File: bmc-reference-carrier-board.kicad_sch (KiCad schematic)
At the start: 0 parts

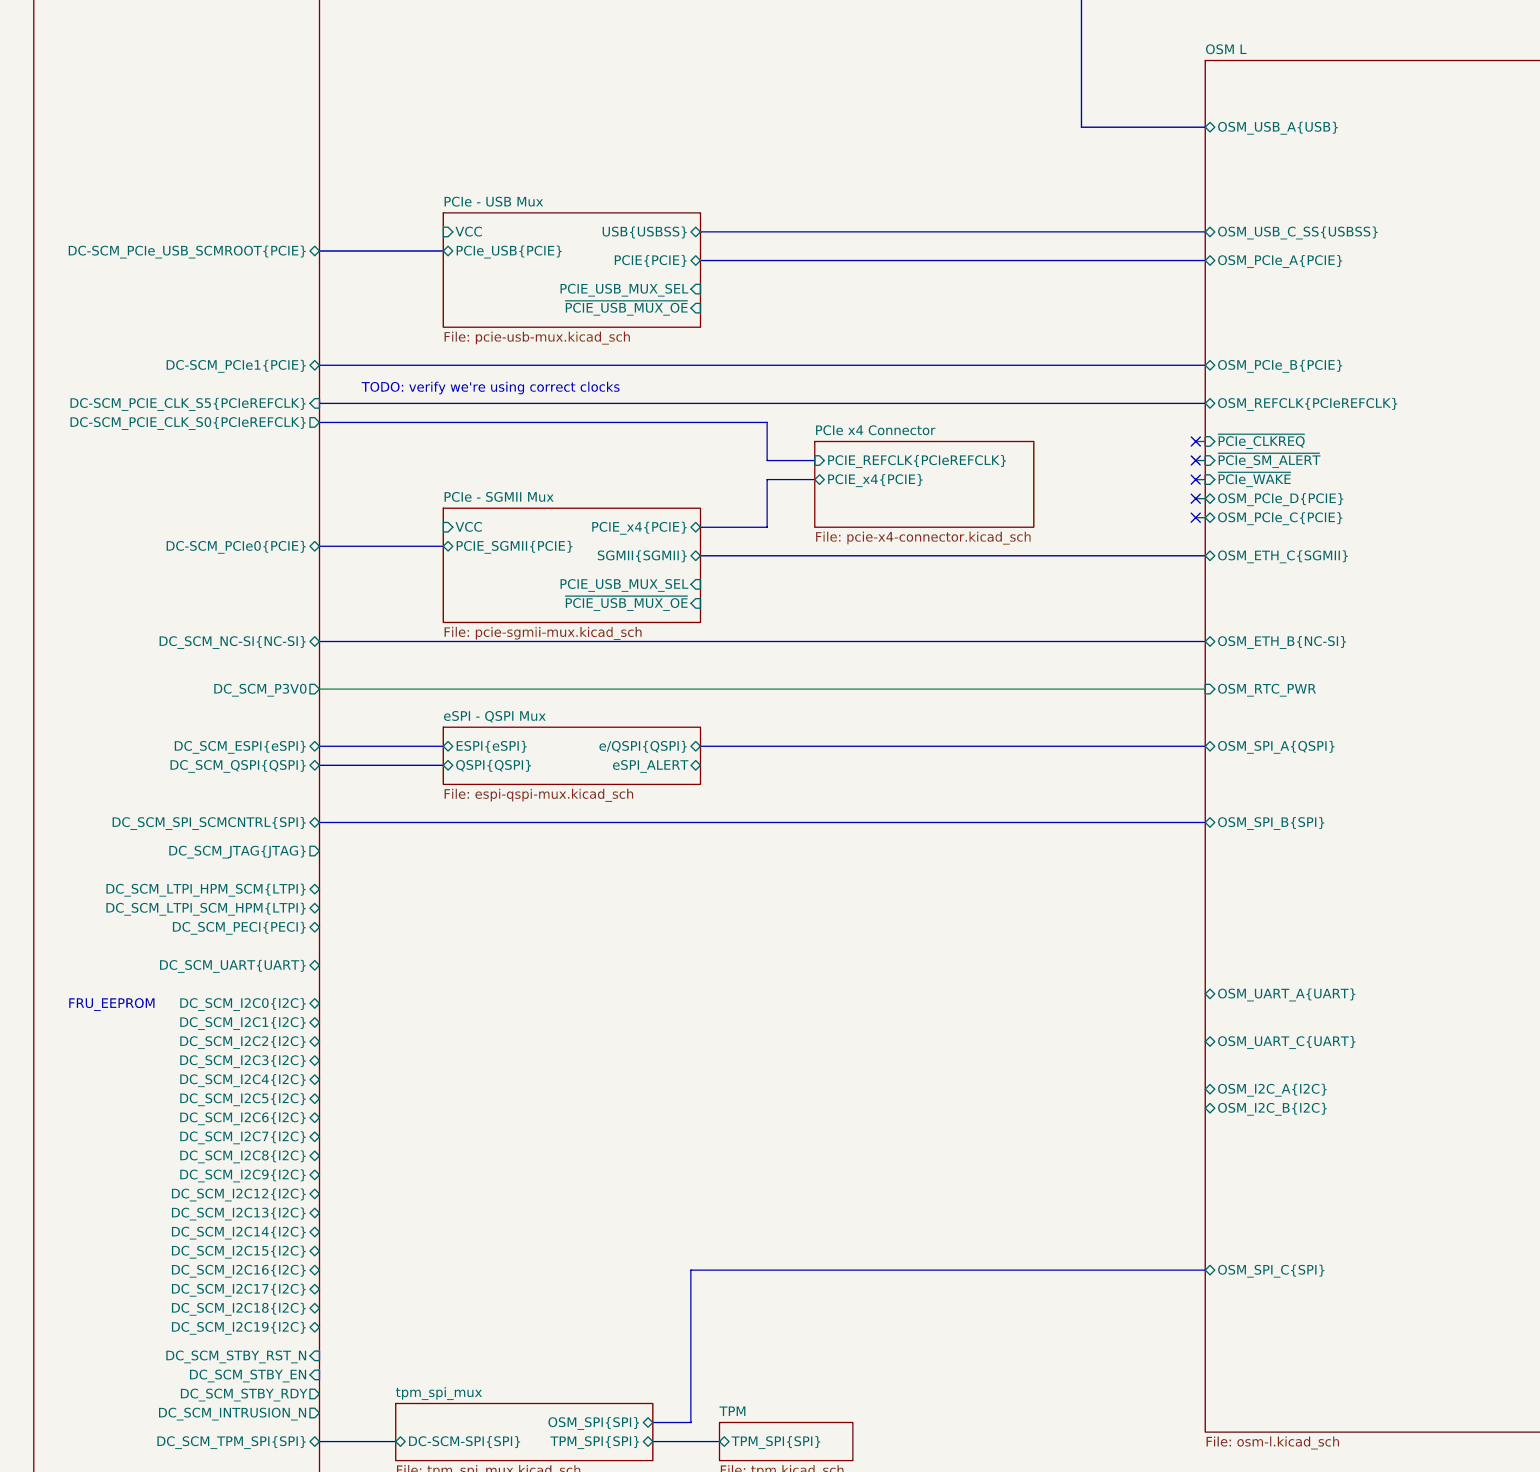
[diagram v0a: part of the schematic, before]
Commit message: [#82323] Add PCIeREFCLK bus, update DC-SCM labels
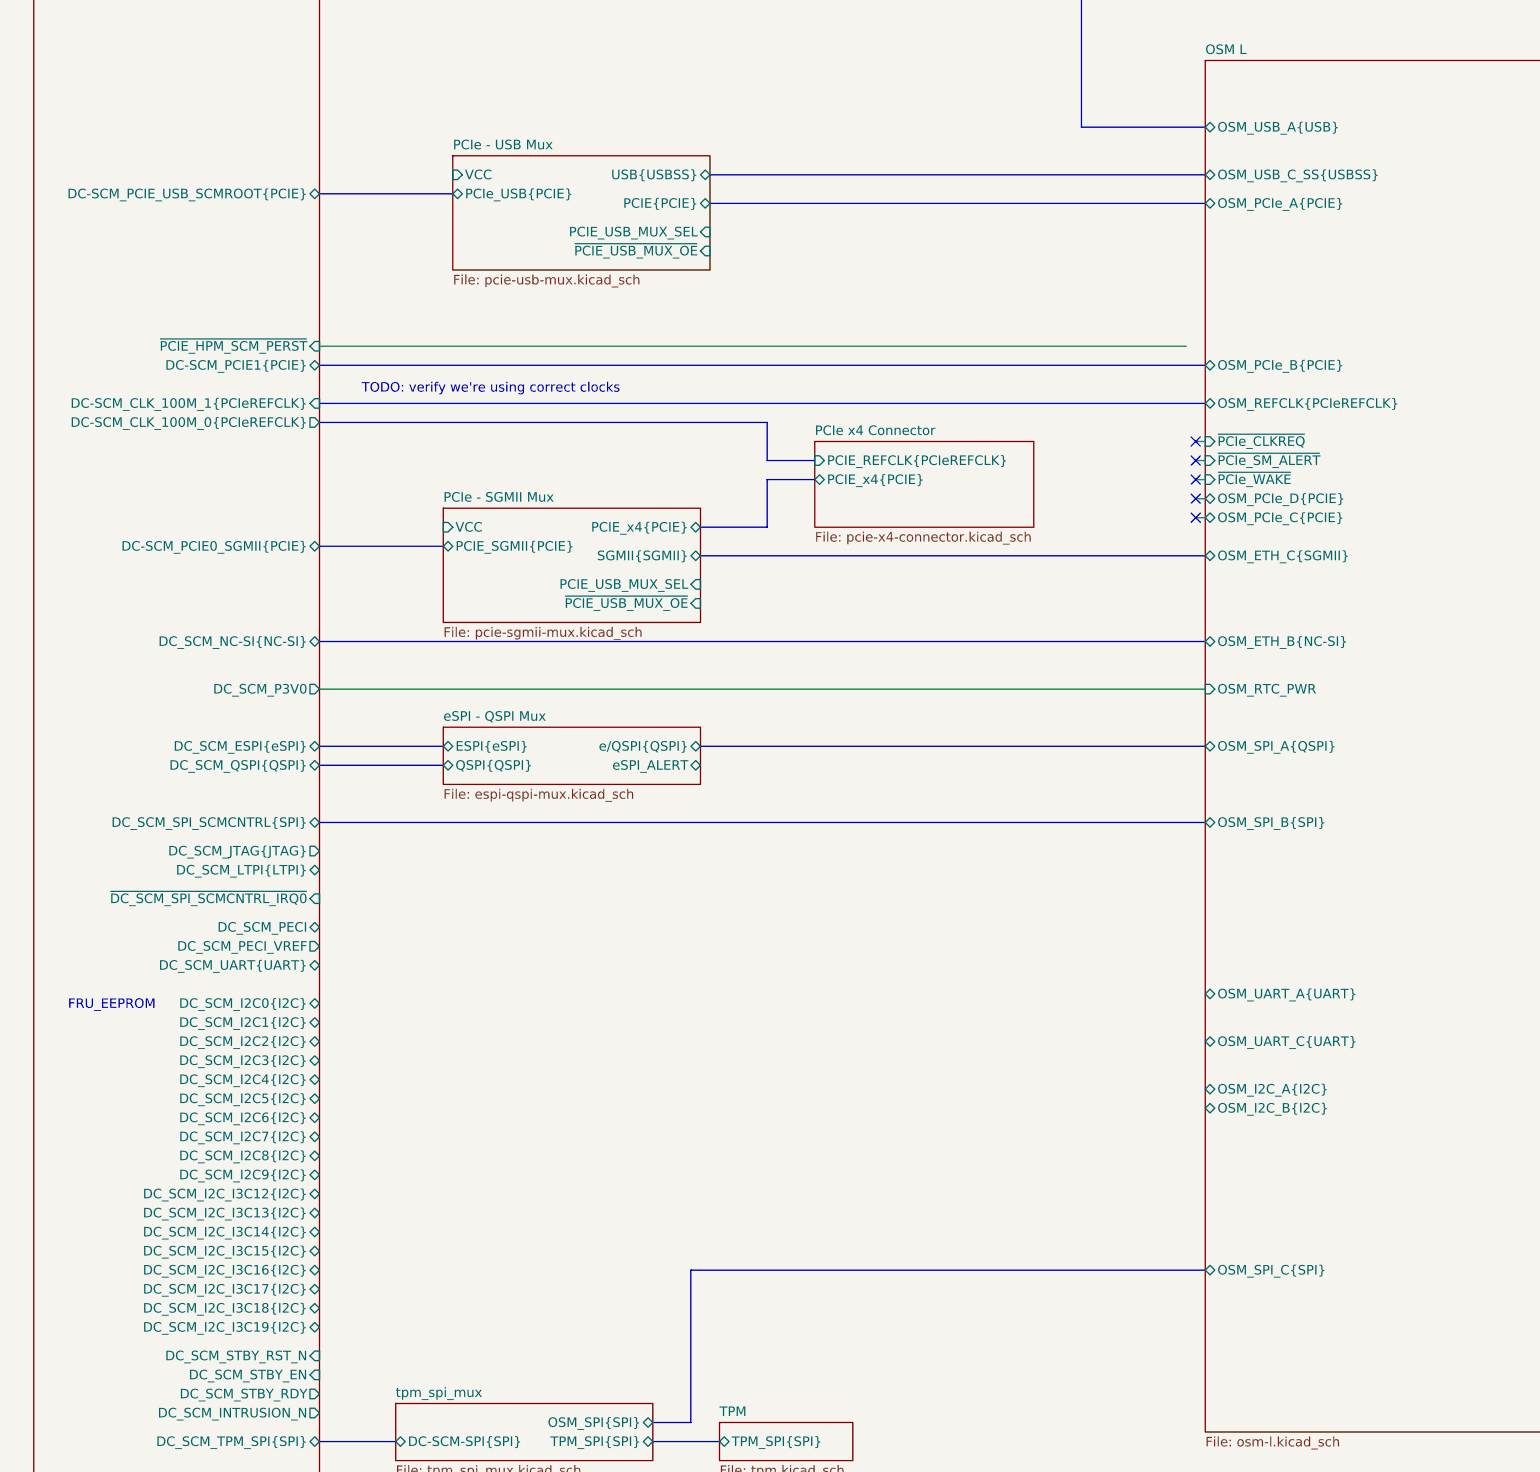
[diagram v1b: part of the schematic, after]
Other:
- sheet DC-SCM 2.1 connector ports: added DC-SCM_CLK_100M_0{PCIeREFCLK}, DC-SCM_CLK_100M_1{PCIeREFCLK}, DC-SCM_PCIE0_SGMII{PCIE}, DC-SCM_PCIE1{PCIE}, DC-SCM_PCIE_USB_SCMROOT{PCIE}, DC_SCM_I2C_I3C12{I2C}, DC_SCM_I2C_I3C13{I2C}, DC_SCM_I2C_I3C14{I2C}, DC_SCM_I2C_I3C15{I2C}, DC_SCM_I2C_I3C16{I2C}, DC_SCM_I2C_I3C17{I2C}, DC_SCM_I2C_I3C18{I2C}, DC_SCM_I2C_I3C19{I2C}, DC_SCM_LTPI{LTPI}, DC_SCM_PECI, DC_SCM_PECI_VREF, ~{DC_SCM_SPI_SCMCNTRL_IRQ0}, ~{PCIE_HPM_SCM_PERST}; removed DC-SCM_PCIE_CLK_S0{PCIeREFCLK}, DC-SCM_PCIE_CLK_S5{PCIeREFCLK}, DC-SCM_PCIe0{PCIE}, DC-SCM_PCIe1{PCIE}, DC-SCM_PCIe_USB_SCMROOT{PCIE}, DC_SCM_I2C12{I2C}, DC_SCM_I2C13{I2C}, DC_SCM_I2C14{I2C}, DC_SCM_I2C15{I2C}, DC_SCM_I2C16{I2C}, DC_SCM_I2C17{I2C}, DC_SCM_I2C18{I2C}, DC_SCM_I2C19{I2C}, DC_SCM_LTPI_HPM_SCM{LTPI}, DC_SCM_LTPI_SCM_HPM{LTPI}, DC_SCM_PECI{PECI}
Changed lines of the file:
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@@
 		)
+	)
+	(bus_alias "PCIeREFCLK"
+		(members "CLK+" "CLK-")
 	)
 	(bus_alias "QSPI"
@@
 	(bus
 		(pts
-			(xy 109.22 109.22) (xy 176.53 109.22)
+			(xy 110.49 101.6) (xy 176.53 101.6)
 		)
 		(stroke
@@
 		)
 	)
-	(bus
-		(pts
-			(xy 58.42 111.76) (xy 74.93 111.76)
+	(wire
+		(pts
+			(xy 58.42 124.46) (xy 173.99 124.46)
+		)
+		(stroke
+			(width 0)
+			(type default)
+		)
+	)
+	(bus
+		(pts
+			(xy 58.42 104.14) (xy 76.2 104.14)
 		)
 		(stroke
@@
 	(bus
 		(pts
-			(xy 109.22 113.03) (xy 176.53 113.03)
+			(xy 110.49 105.41) (xy 176.53 105.41)
 		)
 		(stroke
@@
 	)
 	(sheet
-		(at 74.93 106.68)
+		(at 76.2 99.06)
 		(size 34.29 15.24)
 		(exclude_from_sim no)
@@
 		)
 		(property "Sheetname" "PCIe - USB Mux"
-			(at 74.93 105.9684 0)
+			(at 76.2 98.3484 0)
 			(effects
 				(font
@@
 		)
 		(property "Sheetfile" "pcie-usb-mux.kicad_sch"
-			(at 74.93 122.5046 0)
+			(at 76.2 114.8846 0)
 			(effects
 				(font
@@
 		)
 		(pin "PCIE{PCIE}" bidirectional
-			(at 109.22 113.03 0)
+			(at 110.49 105.41 0)
 			(effects
 				(font
@@
 		)
 		(pin "PCIe_USB{PCIE}" bidirectional
-			(at 74.93 111.76 180)
+			(at 76.2 104.14 180)
 			(effects
 				(font
@@
 		)
 		(pin "USB{USBSS}" bidirectional
-			(at 109.22 109.22 0)
+			(at 110.49 101.6 0)
 			(effects
 				(font
@@
 		)
 		(pin "PCIE_USB_MUX_SEL" input
-			(at 109.22 116.84 0)
+			(at 110.49 109.22 0)
 			(effects
 				(font
@@
 		)
 		(pin "~{PCIE_USB_MUX_OE}" input
-			(at 109.22 119.38 0)
+			(at 110.49 111.76 0)
 			(effects
 				(font
@@
 		)
 		(pin "VCC" input
-			(at 74.93 109.22 180)
+			(at 76.2 101.6 180)
 			(effects
 				(font
@@
 		)
 		(pin "OSM_PCIe_A{PCIE}" bidirectional
-			(at 176.53 113.03 180)
+			(at 176.53 105.41 180)
 			(effects
 				(font
@@
 		)
 		(pin "OSM_USB_C_SS{USBSS}" bidirectional
-			(at 176.53 109.22 180)
+			(at 176.53 101.6 180)
 			(effects
 				(font
@@
 			)
 		)
-		(pin "DC_SCM_I2C13{I2C}" bidirectional
-			(at 58.42 240.03 0)
-			(effects
-				(font
-					(size 1.27 1.27)
-				)
-				(justify right)
-			)
-		)
 		(pin "DC_SCM_I2C5{I2C}" bidirectional
 			(at 58.42 224.79 0)
@@
 			)
 		)
-		(pin "DC_SCM_I2C12{I2C}" bidirectional
-			(at 58.42 237.49 0)
-			(effects
-				(font
-					(size 1.27 1.27)
-				)
-				(justify right)
-			)
-		)
-		(pin "DC_SCM_LTPI_SCM_HPM{LTPI}" bidirectional
-			(at 58.42 199.39 0)
-			(effects
-				(font
-					(size 1.27 1.27)
-				)
-				(justify right)
-			)
-		)
-		(pin "DC_SCM_LTPI_HPM_SCM{LTPI}" bidirectional
-			(at 58.42 196.85 0)
-			(effects
-				(font
-					(size 1.27 1.27)
-				)
-				(justify right)
-			)
-		)
 		(pin "DC_SCM_ESPI{eSPI}" bidirectional
 			(at 58.42 177.8 0)
@@
 			)
 		)
-		(pin "DC_SCM_PECI{PECI}" bidirectional
-			(at 58.42 201.93 0)
-			(effects
-				(font
-					(size 1.27 1.27)
-				)
-				(justify right)
-			)
-		)
 		(pin "DC_SCM_USB1{USB}" bidirectional
 			(at 58.42 34.29 0)
@@
 			)
 		)
-		(pin "DC_SCM_I2C14{I2C}" bidirectional
-			(at 58.42 242.57 0)
-			(effects
-				(font
-					(size 1.27 1.27)
-				)
-				(justify right)
-			)
-		)
-		(pin "DC_SCM_I2C15{I2C}" bidirectional
-			(at 58.42 245.11 0)
-			(effects
-				(font
-					(size 1.27 1.27)
-				)
-				(justify right)
-			)
-		)
-		(pin "DC_SCM_I2C16{I2C}" bidirectional
-			(at 58.42 247.65 0)
-			(effects
-				(font
-					(size 1.27 1.27)
-				)
-				(justify right)
-			)
-		)
-		(pin "DC_SCM_I2C17{I2C}" bidirectional
-			(at 58.42 250.19 0)
-			(effects
-				(font
-					(size 1.27 1.27)
-				)
-				(justify right)
-			)
-		)
-		(pin "DC_SCM_I2C18{I2C}" bidirectional
-			(at 58.42 252.73 0)
-			(effects
-				(font
-					(size 1.27 1.27)
-				)
-				(justify right)
-			)
-		)
-		(pin "DC_SCM_I2C19{I2C}" bidirectional
-			(at 58.42 255.27 0)
-			(effects
-				(font
-					(size 1.27 1.27)
-				)
-				(justify right)
-			)
-		)
-		(pin "DC-SCM_PCIe_USB_SCMROOT{PCIE}" bidirectional
-			(at 58.42 111.76 0)
-			(effects
-				(font
-					(size 1.27 1.27)
-				)
-				(justify right)
-			)
-		)
-		(pin "DC-SCM_PCIE_CLK_S0{PCIeREFCLK}" output
-			(at 58.42 134.62 0)
-			(effects
-				(font
-					(size 1.27 1.27)
-				)
-				(justify right)
-			)
-		)
-		(pin "DC-SCM_PCIE_CLK_S5{PCIeREFCLK}" input
-			(at 58.42 132.08 0)
-			(effects
-				(font
-					(size 1.27 1.27)
-				)
-				(justify right)
-			)
-		)
-		(pin "DC-SCM_PCIe1{PCIE}" bidirectional
-			(at 58.42 127 0)
-			(effects
-				(font
-					(size 1.27 1.27)
-				)
-				(justify right)
-			)
-		)
-		(pin "DC-SCM_PCIe0{PCIE}" bidirectional
-			(at 58.42 151.13 0)
-			(effects
-				(font
-					(size 1.27 1.27)
-				)
-				(justify right)
-			)
-		)
 		(pin "DC_SCM_INTRUSION_N" output
 			(at 58.42 266.7 0)
@@
 			(effects
 				(font
+					(size 1.27 1.27)
+				)
+				(justify right)
+			)
+		)
+		(pin "DC_SCM_I2C_I3C12{I2C}" bidirectional
+			(at 58.42 237.49 0)
+			(effects
+				(font
+					(size 1.27 1.27)
+				)
+				(justify right)
+			)
+		)
+		(pin "DC_SCM_I2C_I3C13{I2C}" bidirectional
+			(at 58.42 240.03 0)
+			(effects
+				(font
+					(size 1.27 1.27)
+				)
+				(justify right)
+			)
+		)
+		(pin "DC_SCM_I2C_I3C14{I2C}" bidirectional
+			(at 58.42 242.57 0)
+			(effects
+				(font
+					(size 1.27 1.27)
+				)
+				(justify right)
+			)
+		)
+		(pin "DC_SCM_I2C_I3C15{I2C}" bidirectional
+			(at 58.42 245.11 0)
+			(effects
+				(font
+					(size 1.27 1.27)
+				)
+				(justify right)
+			)
+		)
+		(pin "DC_SCM_I2C_I3C16{I2C}" bidirectional
+			(at 58.42 247.65 0)
+			(effects
+				(font
+					(size 1.27 1.27)
+				)
+				(justify right)
+			)
+		)
+		(pin "DC_SCM_I2C_I3C17{I2C}" bidirectional
+			(at 58.42 250.19 0)
+			(effects
+				(font
+					(size 1.27 1.27)
+				)
+				(justify right)
+			)
+		)
+		(pin "DC_SCM_I2C_I3C18{I2C}" bidirectional
+			(at 58.42 252.73 0)
+			(effects
+				(font
+					(size 1.27 1.27)
+				)
+				(justify right)
+			)
+		)
+		(pin "DC_SCM_I2C_I3C19{I2C}" bidirectional
+			(at 58.42 255.27 0)
+			(effects
+				(font
+					(size 1.27 1.27)
+				)
+				(justify right)
+			)
+		)
+		(pin "DC_SCM_LTPI{LTPI}" bidirectional
+			(at 58.42 194.31 0)
+			(effects
+				(font
+					(size 1.27 1.27)
+				)
+				(justify right)
+			)
+		)
+		(pin "DC_SCM_PECI" bidirectional
+			(at 58.42 201.93 0)
+			(effects
+				(font
+					(size 1.27 1.27)
+				)
+				(justify right)
+			)
+		)
+		(pin "DC_SCM_PECI_VREF" output
+			(at 58.42 204.47 0)
+			(effects
+				(font
+					(size 1.27 1.27)
+				)
+				(justify right)
+			)
+		)
+		(pin "~{DC_SCM_SPI_SCMCNTRL_IRQ0}" input
+			(at 58.42 198.12 0)
+			(effects
+				(font
+					(size 1.27 1.27)
+				)
+				(justify right)
+			)
+		)
+		(pin "DC-SCM_CLK_100M_0{PCIeREFCLK}" output
+			(at 58.42 134.62 0)
+			(effects
+				(font
+					(size 1.27 1.27)
+				)
+				(justify right)
+			)
+		)
+		(pin "DC-SCM_CLK_100M_1{PCIeREFCLK}" input
+			(at 58.42 132.08 0)
+			(effects
+				(font
+					(size 1.27 1.27)
+				)
+				(justify right)
+			)
+		)
+		(pin "DC-SCM_PCIE0_SGMII{PCIE}" bidirectional
+			(at 58.42 151.13 0)
+			(effects
+				(font
+					(size 1.27 1.27)
+				)
+				(justify right)
+			)
+		)
+		(pin "DC-SCM_PCIE1{PCIE}" bidirectional
+			(at 58.42 127 0)
+			(effects
+				(font
+					(size 1.27 1.27)
+				)
+				(justify right)
+			)
+		)
+		(pin "DC-SCM_PCIE_USB_SCMROOT{PCIE}" bidirectional
+			(at 58.42 104.14 0)
+			(effects
+				(font
+					(size 1.27 1.27)
+				)
+				(justify right)
+			)
+		)
+		(pin "~{PCIE_HPM_SCM_PERST}" input
+			(at 58.42 124.46 0)
+			(effects
+				(font
